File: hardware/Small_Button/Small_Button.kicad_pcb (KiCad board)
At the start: 2 copper layers, 23.2 x 23.2 mm, 5 parts, among them J1 JST PH, SW1 Cherry MX

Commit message: insert summary here
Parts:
- added H3: M2, MountingHole:MountingHole_2.2mm_M2_DIN965, F.Cu at (100.0, 108.5)
- added R1: 0R0, Resistor_SMD:R_0603_1608Metric, B.Cu at (104.5, 105.1)
- J1: footprint Connector_JST:JST_SH_SM04B-SRSS-TB_1x04-1MP_P1.00mm_Horizontal -> Connector_JST:JST_SH_SM03B-SRSS-TB_1x03-1MP_P1.00mm_Horizontal
- moved J1 0.83 mm to (98.1, 93.0), turned to 15.5 degrees
- moved H1 0.75 mm to (91.5, 100.0)
- moved H2 0.75 mm to (108.5, 100.0)
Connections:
- net /LED+ renamed /LED
- D1 pad 1: /LED- -> Net-(D1-K)
- J1 pad 2: /LED- -> /SW
- J1 pad 3: /SW+ -> GND
- SW1 pad 1: /SW+ -> /SW
- SW1 pad 2: /SW- -> GND
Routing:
- net /LED-: track 15.3 -> 0.00 mm
- net /SW-: track 9.15 -> 0.00 mm
- net /SW: track 0.00 -> 5.91 mm
- net /LED: track 16.2 -> 10.9 mm
- net /SW+: track 4.67 -> 0.00 mm
- net Net-(D1-K): track 0.00 -> 2.35 mm
- net GND: vias 12 -> 11
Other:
- board size 23.2 x 23.2 mm -> 20.8 x 20.9 mm

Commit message: Update Small Button PCB
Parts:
- R1: value 0R0 -> 100Ω
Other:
- board text added: "0"
- board text added: "0 mm"
- board text added: "0.01 mm"
- board text added: "0.02"
- board text added: "0.035 mm"
- board text added: "0.2032 mm / 0.2032 mm"
- board text added: "0.3000 mm"
- board text added: "1"
- board text added: "1.51 mm"
- board text added: "1.6000 mm"
- board text added: "2"
- board text added: "20.8000 mm x 20.8690 mm"
- board text added: "3.3"
- board text added: "4.5"
- board text added: "B.Cu"
- board text added: "B.Mask"
- board text added: "B.Paste"
- board text added: "B.Silkscreen"
- board text added: "BOARD CHARACTERISTICS"
- board text added: "Black"
- board text added: "Board Thickness:"
- board text added: "Board overall dimensions:"
- board text added: "Bottom Silk Screen"
- board text added: "Bottom Solder Mask"
- board text added: "Bottom Solder Paste"
- board text added: "Castellated pads:"
- board text added: "Color"
- board text added: "Copper Finish:"
- board text added: "Copper Layer Count:"
- board text added: "Dielectric 1"
- board text added: "Direct Printing"
- board text added: "ENIG"
- board text added: "Edge card connectors:"
- board text added: "Epoxy"
- board text added: "Epsilon R"
- board text added: "F.Cu"
- board text added: "F.Mask"
- board text added: "F.Paste"
- board text added: "F.Silkscreen"
- board text added: "FR4"
- board text added: "FR4 natural"
- board text added: "Impedance Control:"
- board text added: "Layer Name"
- board text added: "Loss Tangent"
- board text added: "Material"
- board text added: "Min hole diameter:"
- board text added: "Min track/spacing:"
- board text added: "No"
- board text added: "Plated Board Edge:"
- board text added: "Thickness (mm)"
- board text added: "Top Silk Screen"
- board text added: "Top Solder Mask"
- board text added: "Top Solder Paste"
- board text added: "Type"
- board text added: "White"
- board text added: "copper"
- board text added: "core"

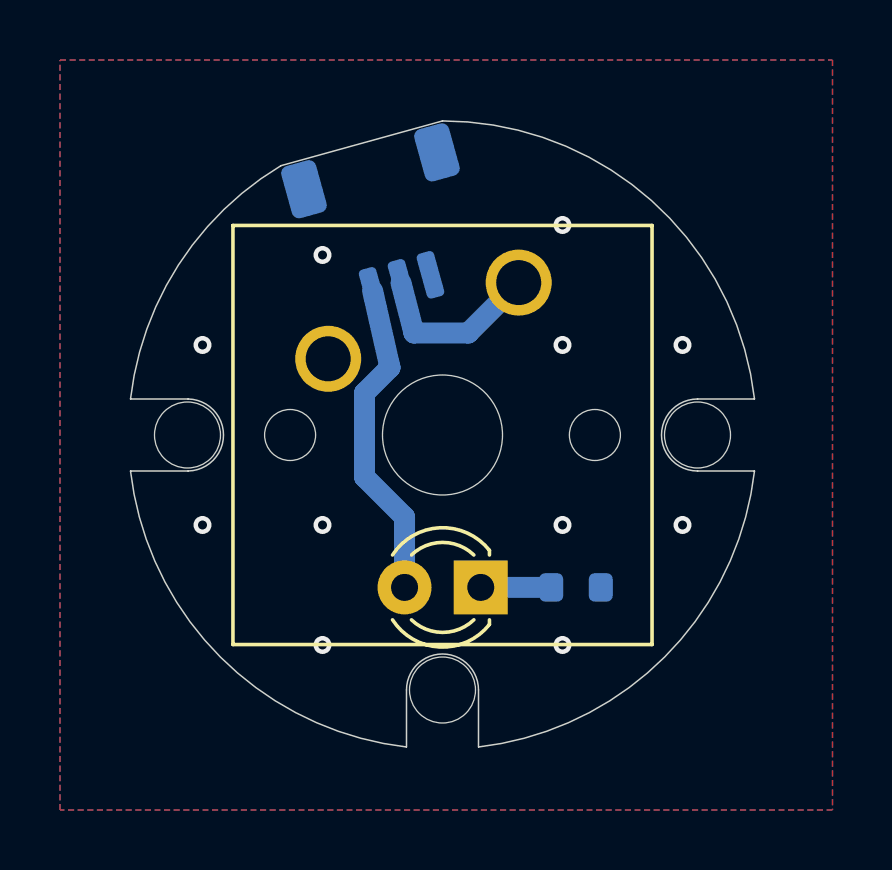
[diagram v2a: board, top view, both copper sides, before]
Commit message: Update Large Button PCB
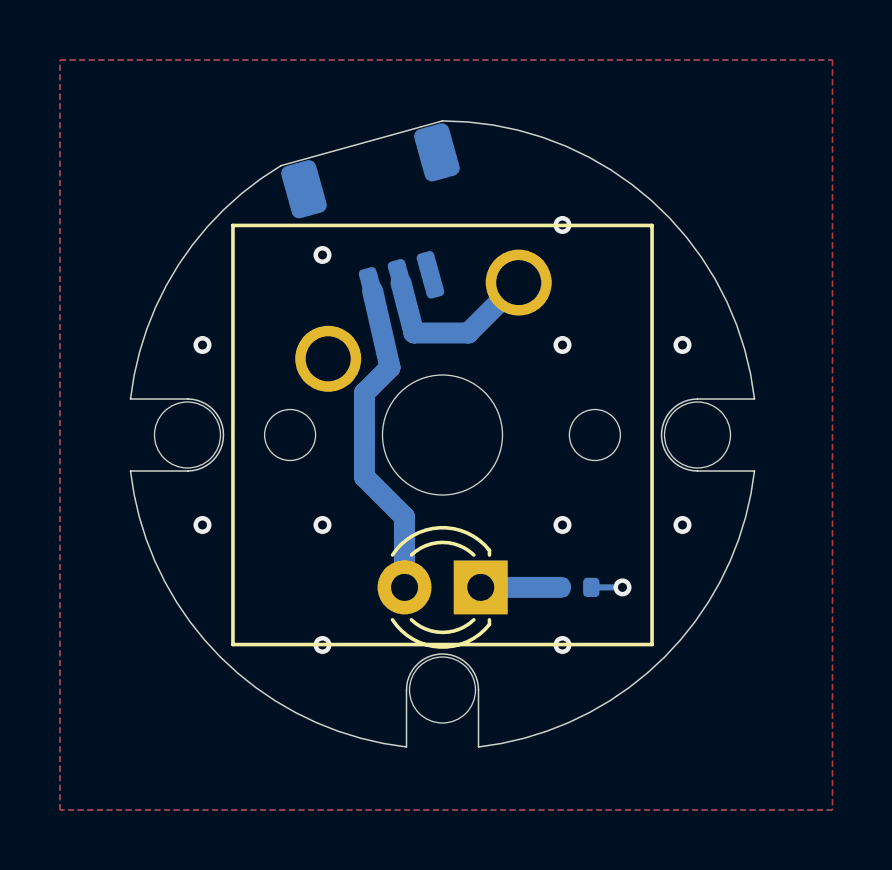
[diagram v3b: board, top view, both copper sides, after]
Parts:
- J1: value JST PH -> JST SH
- R1: footprint Resistor_SMD:R_0603_1608Metric -> Resistor_SMD:R_0402_1005Metric
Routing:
- net GND: track 0.00 -> 1.04 mm, vias 11 -> 12
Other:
- board text added: "Blue"
- board text removed: "Black"
